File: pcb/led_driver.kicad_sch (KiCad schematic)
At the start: 3 parts, among them Q1 AO3400A

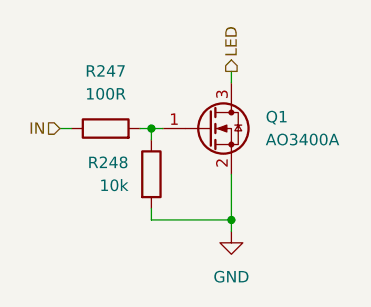
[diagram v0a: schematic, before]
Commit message: Updated the schematic to use dual red/yellow LEDs
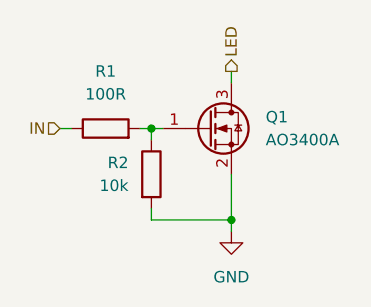
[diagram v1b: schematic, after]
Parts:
- renumbered R247 to R1, R248 to R2

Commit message: Circuit rewrite to put LEDs closer together for the shift registers
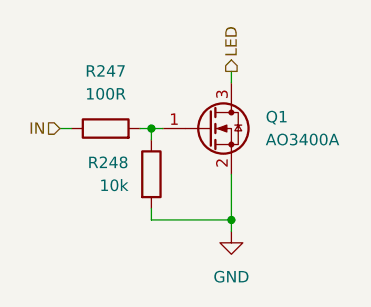
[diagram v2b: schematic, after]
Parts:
- renumbered R1 to R247, R2 to R248

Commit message: PCB track routing part 5
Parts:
- renumbered R247 to R245, R248 to R246
